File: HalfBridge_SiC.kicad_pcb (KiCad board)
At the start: 2 copper layers, 100 x 100.3 mm, 67 parts, among them J1 Conn_02x08_Odd_Even, J2 AFBR-2624Z, J3 AFBR-2624Z, J4 Screw_Terminal_01x02, J5 Conn_01x04_Shielded, Q1 C3M0075120J, Q2 C3M0075120J, SW1 CAS-D20X1, SW2 CAS-D20X1, SW3 CAS-D20X1, U1 RKD-052005D, U2 RKD-052005D, U3 MAX3284E, U4 NCD57252, U5 MAX3284E, U6 74AUC2GU04

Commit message: new optical diff xor
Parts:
- removed the C15 at (49.6, 100.6)
- removed the C17 at (49.5, 66.0)
- removed the C2 at (54.0, 86.5)
- removed the C3 at (54.0, 81.0)
- removed the J2 at (51.5, 61.9)
- removed the L1 at (44.5, 67.5)
- removed the R14 at (55.0, 51.6)
- removed the R15 at (54.9, 62.0)
- removed the R18 at (48.0, 85.5)
- removed SW3: CAS-D20X1, My_Button_Switch_SMD:Nidec_Copal_CAS-D20A1
- removed the U5 at (50.7, 80.0)
- removed the U6 at (53.0, 75.5)
- added C23: C, Capacitor_SMD:C_0805_2012Metric_Pad1.18x1.45mm_HandSolder, F.Cu at (46.0, 78.5)
- added C24: C, Capacitor_SMD:C_0805_2012Metric_Pad1.18x1.45mm_HandSolder, F.Cu at (45.0, 62.1)
- added C25: C, Capacitor_SMD:C_0805_2012Metric_Pad1.18x1.45mm_HandSolder, F.Cu at (45.0, 51.2)
- added C27: 100n, Capacitor_SMD:C_0603_1608Metric_Pad1.08x0.95mm_HandSolder, F.Cu at (22.8, 37.0)
- added C28: 100n, Capacitor_SMD:C_0603_1608Metric_Pad1.08x0.95mm_HandSolder, F.Cu at (22.8, 39.5)
- added C4: C, Capacitor_SMD:C_0603_1608Metric_Pad1.08x0.95mm_HandSolder, F.Cu at (49.6, 100.6)
- added D2: LED, LED_SMD:LED_0603_1608Metric_Pad1.05x0.95mm_HandSolder, F.Cu at (43.3, 95.5)
- added D3: LED, LED_SMD:LED_0603_1608Metric_Pad1.05x0.95mm_HandSolder, F.Cu at (43.3, 99.5)
- added D4: LED, LED_SMD:LED_0603_1608Metric_Pad1.05x0.95mm_HandSolder, F.Cu at (43.3, 103.5)
- added J4: AFBR-2624Z, OptoDevice:Broadcom_AFBR-16xxZ_Vertical, B.Cu at (49.5, 50.2)
- added J6: Conn_01x04_Shielded, My_Connector:Samtec_T1M-04-X-SH-L_1x04-1SH_P1.0mm_Terminal_Horizontal_Latch, F.Cu at (32.7, 38.0)
- added J7: Conn_01x02, Connector_PinHeader_2.54mm:PinHeader_1x02_P2.54mm_Vertical_SMD_Pin1Right, B.Cu at (61.0, 56.0)
- added L3: L, Inductor_SMD:L_0603_1608Metric_Pad1.05x0.95mm_HandSolder, F.Cu at (43.5, 55.2)
- added L4: L, Inductor_SMD:L_0603_1608Metric_Pad1.05x0.95mm_HandSolder, F.Cu at (43.5, 76.0)
- added R20: R, Resistor_SMD:R_0603_1608Metric_Pad0.98x0.95mm_HandSolder, F.Cu at (52.0, 51.2)
- added R21: R, Resistor_SMD:R_0603_1608Metric_Pad0.98x0.95mm_HandSolder, F.Cu at (52.0, 72.5)
- added R22: R, Resistor_SMD:R_0603_1608Metric_Pad0.98x0.95mm_HandSolder, F.Cu at (22.8, 42.0)
- added R23: R, Resistor_SMD:R_0603_1608Metric_Pad0.98x0.95mm_HandSolder, F.Cu at (22.8, 44.6)
- added R4: R, Resistor_SMD:R_0603_1608Metric, F.Cu at (45.0, 95.0)
- added R5: R, Resistor_SMD:R_0603_1608Metric, F.Cu at (45.0, 99.2)
- added R6: R, Resistor_SMD:R_0603_1608Metric, F.Cu at (45.0, 103.0)
- added U1: 74AHC1G86, Package_TO_SOT_SMD:SOT-23-5_HandSoldering, F.Cu at (52.0, 88.5)
- added U2: 74AHC1G86, Package_TO_SOT_SMD:SOT-23-5_HandSoldering, F.Cu at (48.0, 88.5)
- added U7: MAX3284E, Package_TO_SOT_SMD:SOT-23-6_Handsoldering, B.Cu at (29.6, 62.5)
- added U8: MAX3284E, Package_TO_SOT_SMD:SOT-23-6_Handsoldering, F.Cu at (55.1, 55.5)
- C18, C19: footprint Capacitor_SMD:C_0805_2012Metric_Pad1.18x1.45mm_HandSolder -> Capacitor_SMD:C_0603_1608Metric_Pad1.08x0.95mm_HandSolder
- C26: value 100n -> C; footprint Capacitor_SMD:C_0603_1608Metric_Pad1.08x0.95mm_HandSolder -> Capacitor_SMD:C_0805_2012Metric_Pad1.18x1.45mm_HandSolder
- J3: footprint OptoDevice:Broadcom_AFBR-16xxZ_Horizontal -> OptoDevice:Broadcom_AFBR-16xxZ_Vertical
- J5: value Conn_01x04_Shielded -> AFBR-2624Z; footprint My_Connector:Samtec_T1M-04-X-SH-L_1x04-1SH_P1.0mm_Terminal_Horizontal_Latch -> OptoDevice:Broadcom_AFBR-16xxZ_Vertical; moved to B.Cu
- R19: moved to F.Cu
- U3: value MAX3284E -> 74AHC1G86; footprint Package_TO_SOT_SMD:SOT-23-6_Handsoldering -> Package_TO_SOT_SMD:SOT-23-5_HandSoldering
- moved SW2 34.2 mm to (43.5, 109.2), turned to 90 degrees
- moved C20 19.5 mm to (48.0, 75.0)
- moved R19 18.4 mm to (52.0, 62.1)
- moved C21 12.7 mm to (46.0, 68.1), turned to -90 degrees
- moved J5 12.4 mm to (49.5, 71.4), turned to 180 degrees
- moved C26 12.2 mm to (45.0, 72.5), turned to 0 degrees
- moved C19 12.1 mm to (48.0, 53.7)
- moved J3 9.46 mm to (49.5, 60.9)
- moved L2 8.56 mm to (43.5, 65.6), turned to 90 degrees
- moved U3 7.30 mm to (44.0, 88.5), turned to -90 degrees
- moved C22 5.06 mm to (46.0, 57.7), turned to -90 degrees
- moved R9 3.13 mm to (47.2, 107.5), turned to 90 degrees
- moved SW1 2.05 mm to (43.5, 115.0)
- moved C18 1.46 mm to (48.0, 64.6)
- moved C16 0.50 mm to (66.0, 100.0)
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- renumbered C9 to C10, C10 to C11, C7 to C12, C8 to C13, C13 to C14, C14 to C15, C11 to C16, C12 to C17, C4 to C2, C5 to C3, C16 to C5, C23 to C6, C24 to C7, C6 to C8, C25 to C9, D3 to D1, D1 to D5, D2 to D6, J4 to J1, J1 to J2, L3 to L1, R17 to R1, R11 to R10, R3 to R11, R4 to R12, R5 to R13, R6 to R14, R7 to R15, R8 to R16, R9 to R17, R10 to R18, R1 to R2, R2 to R3, R12 to R7, R13 to R8, R16 to R9, U1 to U4, U4 to U5, U2 to U6
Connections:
- C19 pad 1: /HalfBridge_Diff/vcc -> /HalfBridge_Optical/vcca
- C20 pad 1: /HalfBridge_Optical/vcca -> /HalfBridge_Optical/vccen
- C21 pad 1: /HalfBridge_Optical/vcca -> /HalfBridge_Optical/vccb
- C22 pad 1: /HalfBridge_Diff/vcc -> /HalfBridge_Optical/vcca
- C26 pad 1: /HalfBridge_Diff/gnd -> /HalfBridge_Diff/vcc
- C26 pad 2: /HalfBridge_Diff/vcc -> /HalfBridge_Diff/gnd
- C9 pad 1: /HalfBridge_GateDriver/rdt -> /HalfBridge_GateDriver/dt
- J3 pad 1: /HalfBridge_Optical/xna -> /HalfBridge_Optical/oinb
- J3 pad 3: /HalfBridge_Optical/vcca -> /HalfBridge_Optical/vccb
- J5 pad 1: /HalfBridge_Diff/inb_db -> /HalfBridge_Optical/oinen
- J5 pad 2: /HalfBridge_Diff/inb_da -> /HalfBridge_Diff/gnd
- J5 pad 3: /HalfBridge_Diff/ina_db -> /HalfBridge_Optical/vccen
- J5 pad 4: /HalfBridge_Diff/ina_da -> unconnected-(J5-NC-Pad4)
- L2 pad 1: /HalfBridge_Optical/vcca -> /HalfBridge_Optical/vccb
- R19 pad 1: /HalfBridge_Diff/inb_da -> /HalfBridge_GateDriver/inb
- R19 pad 2: /HalfBridge_Diff/inb_db -> /HalfBridge_Optical/oinb
- R7 pad 1: /HalfBridge_GateDriver/ina -> /HalfBridge_GateDriver/inga
- R8 pad 1: /HalfBridge_GateDriver/inb -> /HalfBridge_GateDriver/ingb
- SW2 pad 1: /HalfBridge_Diff/ina_d -> /HalfBridge_Diff/vcc
- SW2 pad 2: /HalfBridge_GateDriver/ina -> /HalfBridge_GateDriver/dis_i
- SW2 pad 3: /HalfBridge_Optical/ina -> /HalfBridge_Diff/gnd
- SW2 pad 4: /HalfBridge_Diff/inb_d -> /HalfBridge_GateDriver/dis_x
- SW2 pad 5: /HalfBridge_GateDriver/inb -> /HalfBridge_GateDriver/dis
- SW2 pad 6: /HalfBridge_Optical/inb -> /HalfBridge_GateDriver/dis_i
- U3 pad 1: /HalfBridge_Diff/vcc -> /HalfBridge_GateDriver/en
- U3 pad 2: /HalfBridge_Diff/gnd -> unconnected-(U3-Pad2)
- U3 pad 3: /HalfBridge_Diff/ina_nd -> /HalfBridge_Diff/gnd
- U3 pad 4: /HalfBridge_Diff/ina_db -> /HalfBridge_GateDriver/dis_x
- U3 pad 5: unconnected-(U3-VL-Pad5) -> /HalfBridge_Diff/vcc
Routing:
- net /HalfBridge_Diff/vcc: track 152.6 -> 14.4 mm
- net /HalfBridge_GateDriver/ina: track 10.2 -> 48.5 mm
- net /HalfBridge_Optical/ina: track 31.2 -> 0.00 mm
- net /HalfBridge_GateDriver/en: track 0.00 -> 23.6 mm
- net /HalfBridge_Optical/inb: track 20.7 -> 0.00 mm
- net /HalfBridge_GateDriver/inb: track 17.9 -> 36.3 mm
- net /HalfBridge_Diff/inb_d: track 12.5 -> 0.00 mm
- net /HalfBridge_GateDriver/dis: track 0.00 -> 12.3 mm
- net /HalfBridge_GateDriver/dt: track 0.00 -> 11.9 mm
- net /HalfBridge_Diff/ina_nd: track 9.15 -> 0.00 mm
- net /HalfBridge_GateDriver/inga: track 0.00 -> 9.08 mm
- net /HalfBridge_Diff/inb_nd: track 5.86 -> 0.00 mm
- net /HalfBridge_GateDriver/ingb: track 0.00 -> 5.50 mm
- net /HalfBridge_GateDriver/anb: track 0.00 -> 5.38 mm
- net /HalfBridge_GateDriver/dis_i: track 0.00 -> 3.52 mm
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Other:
- board text removed: "INA PWM"
- board text removed: "INB"

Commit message: diff circuit
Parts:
- removed J6: Conn_01x04_Shielded, My_Connector:Samtec_T1M-04-X-SH-L_1x04-1SH_P1.0mm_Terminal_Horizontal_Latch
- added C12: 100n, Capacitor_SMD:C_0603_1608Metric_Pad1.08x0.95mm_HandSolder, F.Cu at (52.0, 115.0)
- added C33: 100n, Capacitor_SMD:C_0603_1608Metric_Pad1.08x0.95mm_HandSolder, F.Cu at (64.0, 78.5)
- added C4: 100n, Capacitor_SMD:C_0603_1608Metric_Pad1.08x0.95mm_HandSolder, F.Cu at (51.5, 92.0)
- added C5: 100n, Capacitor_SMD:C_0603_1608Metric_Pad1.08x0.95mm_HandSolder, F.Cu at (47.5, 92.0)
- added C6: 100n, Capacitor_SMD:C_0603_1608Metric_Pad1.08x0.95mm_HandSolder, F.Cu at (43.5, 92.0)
- added J10: Conn_01x02, Connector_PinHeader_2.54mm:PinHeader_1x02_P2.54mm_Vertical, F.Cu at (63.5, 50.7)
- added J11: Conn_01x02, Connector_PinHeader_2.54mm:PinHeader_1x02_P2.54mm_Vertical, F.Cu at (63.5, 61.2)
- added J12: Conn_01x02, Connector_PinHeader_2.54mm:PinHeader_1x02_P2.54mm_Vertical, F.Cu at (63.5, 72.2)
- added J14: Conn_01x02_Shielded, My_Connector:SAMTEC_T1M-02-F-SV-L-P, B.Cu at (60.4, 67.7)
- added J8: Conn_01x02, Connector_PinHeader_2.54mm:PinHeader_1x02_P2.54mm_Vertical, F.Cu at (54.0, 66.2)
- added J9: Conn_01x02, Connector_PinHeader_2.54mm:PinHeader_1x02_P2.54mm_Vertical, F.Cu at (54.0, 76.7)
- added R24: R, Resistor_SMD:R_0603_1608Metric_Pad0.98x0.95mm_HandSolder, F.Cu at (57.0, 78.5)
- added R25: R, Resistor_SMD:R_0603_1608Metric, F.Cu at (60.5, 52.5)
- added R26: R, Resistor_SMD:R_0603_1608Metric, F.Cu at (60.5, 63.0)
- added R27: R, Resistor_SMD:R_0603_1608Metric, F.Cu at (60.5, 74.0)
- added U9: MAX3284E, Package_TO_SOT_SMD:SOT-23-6_Handsoldering, F.Cu at (60.5, 78.5)
- J7: footprint Connector_PinHeader_2.54mm:PinHeader_1x02_P2.54mm_Vertical_SMD_Pin1Right -> Connector_PinHeader_2.54mm:PinHeader_1x02_P2.54mm_Vertical; moved to F.Cu
- U7: moved to F.Cu
- moved C32 50.1 mm to (64.0, 68.0), turned to 90 degrees
- moved C31 46.0 mm to (64.0, 57.5), turned to 90 degrees
- moved R23 41.5 mm to (57.0, 68.0), turned to 90 degrees
- moved R22 37.6 mm to (57.0, 57.5), turned to 90 degrees
- moved U7 31.1 mm to (60.4, 57.5)
- moved U8 13.6 mm to (60.5, 68.0), turned to 180 degrees
- moved J7 7.04 mm to (54.0, 55.2), turned to 0 degrees
- moved D5 2.50 mm to (72.5, 89.3)
- moved D6 2.00 mm to (72.5, 128.0)
- moved U1 1.50 mm to (50.5, 88.5)
- moved U2 1.50 mm to (46.5, 88.5)
- moved U3 1.50 mm to (42.5, 88.5)
- moved R6 1.17 mm to (45.0, 104.2)
- moved D4 1.04 mm to (43.3, 104.5)
- moved D2 1.00 mm to (43.3, 96.5)
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- renumbered C7 to C10, C8 to C11, C9 to C13, C10 to C14, C11 to C15, C12 to C16, C13 to C17, C14 to C18, C15 to C19, C16 to C20, C17 to C21, C18 to C22, C19 to C23, C20 to C24, C21 to C25, C22 to C26, C23 to C27, C24 to C28, C25 to C29, C26 to C30, C27 to C31, C28 to C32, C4 to C7, C5 to C8, C6 to C9
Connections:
- net /HalfBridge_GateDriver/en renamed /HalfBridge_Diff/inen_d
- net /HalfBridge_GateDriver/ina renamed /HalfBridge_Diff/ina_d
- net /HalfBridge_GateDriver/inb renamed /HalfBridge_Diff/inb_d
- J7 pad 1: unconnected-(J7-Pin_1-Pad1) -> /HalfBridge_Diff/ina_db
- J7 pad 2: unconnected-(J7-Pin_2-Pad2) -> /HalfBridge_Diff/ina_da
- SW2 pad 1: /HalfBridge_Diff/vcc -> /HalfBridge_GateDriver/dis_i
- SW2 pad 2: /HalfBridge_GateDriver/dis_i -> /HalfBridge_GateDriver/dis
- SW2 pad 3: /HalfBridge_Diff/gnd -> /HalfBridge_GateDriver/dis_x
- SW2 pad 4: /HalfBridge_GateDriver/dis_x -> /HalfBridge_Diff/gnd
- SW2 pad 5: /HalfBridge_GateDriver/dis -> /HalfBridge_GateDriver/dis_i
- SW2 pad 6: /HalfBridge_GateDriver/dis_i -> /HalfBridge_Diff/vcc
- U7 pad 5: unconnected-(U7-VL-Pad5) -> /HalfBridge_Diff/vcc
- U8 pad 5: unconnected-(U8-VL-Pad5) -> /HalfBridge_Diff/vcc
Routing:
- net /HalfBridge_Diff/vcc: track 14.4 -> 138.5 mm
- net /HalfBridge_GateDriver/dis_x: track 2.05 -> 18.0 mm
- net /HalfBridge_GateDriver/ingb: track 5.50 -> 21.4 mm
- net /HalfBridge_GateDriver/inga: track 9.08 -> 18.5 mm
- net /HalfBridge_GateDriver/anb: track 5.38 -> 12.2 mm
- net /HalfBridge_Diff/inen_d: track 23.6 -> 20.3 mm
- net /HalfBridge_GateDriver/asgh: track 6.56 -> 4.06 mm
- net /HalfBridge_Diff/ina_d: track 48.5 -> 50.8 mm
- net /HalfBridge_GateDriver/asgl: track 4.27 -> 2.06 mm
- net /HalfBridge_Diff/inb_d: track 36.3 -> 37.8 mm
- net /HalfBridge_GateDriver/dis: track 12.3 -> 13.4 mm
- net /HalfBridge_GateDriver/kl: vias 24 -> 26
- net /HalfBridge_Diff/gnd: vias 0 -> 4
- added copper zone on B.Cu, net /HalfBridge_Diff/gnd
- added copper zone on F.Cu, net /HalfBridge_Diff/gnd
- removed copper zone on B.Cu, net (none)
- removed copper zone on F.Cu, net (none)
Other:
- board size 100 x 100.3 mm -> 100 x 100 mm

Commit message: pcb position
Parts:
- C18, C19, R4, R5, R6: moved to B.Cu
- moved C9 7.38 mm to (50.0, 102.5), turned to 180 degrees
- moved C18 7.02 mm to (66.0, 110.5), turned to 0 degrees
- moved C19 6.02 mm to (66.0, 113.5)
- moved R4 2.92 mm to (42.5, 97.5)
- moved R5 2.69 mm to (42.5, 101.0)
- moved R6 2.52 mm to (42.5, 104.5)
- moved U6 2.19 mm to (50.9, 121.6)
- moved R13 2.00 mm to (75.5, 91.8)
- moved R14 2.00 mm to (75.5, 93.8)
- moved L1 1.93 mm to (51.0, 105.6), turned to -90 degrees
- moved R1 1.66 mm to (44.0, 123.0), turned to 90 degrees
- moved C10 1.58 mm to (51.0, 109.5), turned to -90 degrees
- moved C4 1.00 mm to (51.5, 93.0)
- moved C5 1.00 mm to (47.5, 93.0)
- moved C6 1.00 mm to (43.5, 93.0)
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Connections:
- R1 pad 2: GND -> /HalfBridge_Diff/gnd
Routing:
- net /HalfBridge_Diff/inen_d: track 20.3 -> 47.9 mm
- net /HalfBridge_Diff/inb_d: track 37.8 -> 56.6 mm
- net /HalfBridge_Diff/vcc: track 138.5 -> 156.5 mm
- net /HalfBridge_GateDriver/vcci: track 0.00 -> 16.2 mm, vias 0 -> 3
- net /HalfBridge_GateDriver/vddl: track 2.18 -> 16.4 mm, vias 0 -> 2
- net /HalfBridge_Diff/ina_d: track 50.8 -> 64.8 mm
- net /HalfBridge_GateDriver/vssl: track 2.16 -> 8.23 mm, vias 0 -> 2
- net /HalfBridge_GateDriver/inaf: track 0.00 -> 4.98 mm
- net /HalfBridge_GateDriver/inbf: track 0.00 -> 4.04 mm
- net /HalfBridge_GateDriver/ingb: track 21.4 -> 17.7 mm
- net /HalfBridge_GateDriver/rdt: track 0.36 -> 3.84 mm
- net /HalfBridge_GateDriver/gonl: track 24.8 -> 26.9 mm
- net /HalfBridge_GateDriver/dt: track 11.5 -> 13.3 mm
- net /HalfBridge_GateDriver/dis_x: track 18.0 -> 17.0 mm
- net /HalfBridge_GateDriver/inga: track 18.5 -> 17.9 mm
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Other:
- outline, holes or cut-outs redrawn

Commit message: route
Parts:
- moved J14 4.09 mm to (64.5, 68.0), turned to -90 degrees
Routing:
- net /HalfBridge_GateDriver/gonh: track 7.32 -> 23.6 mm
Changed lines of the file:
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@@
 		(tags "capacitor handsolder")
 		(property "Reference" "C18"
-			(at 0 -1.945 360)
+			(at 0 -1.945 0)
 			(layer "B.SilkS")
 			(effects
@@
 		)
 		(property "Value" "C"
-			(at 0 -1.68 360)
+			(at 0 -1.68 0)
 			(layer "B.Fab")
 			(effects
@@
 		)
 		(fp_text user "${REFERENCE}"
-			(at 0 0 360)
+			(at 0 0 0)
 			(layer "B.Fab")
 			(effects
@@
 		)
 		(property "Value" "C"
-			(at 0 -1.68 360)
+			(at 0 -1.68 0)
 			(layer "B.Fab")
 			(effects
@@
 		)
 		(fp_text user "${REFERENCE}"
-			(at 0 0 360)
+			(at 0 0 0)
 			(layer "B.Fab")
 			(effects
@@
 	(footprint "My_Connector:SAMTEC_T1M-02-F-SV-L-P"
 		(layer "B.Cu")
-		(at 60.425 67.7 90)
+		(at 64.5 68 -90)
 		(descr "1MM TERMINAL STRIP, 5PINS.")
 		(property "Reference" "J14"
@@
 		(attr smd)
 		(fp_line
-			(start 2.2 0.425)
-			(end 2.2 1.3)
+			(start -1 4.375)
+			(end -1 3.175)
 			(stroke
 				(width 0.127)
@@
 		)
 		(fp_line
-			(start 1.25 0.425)
-			(end 1.25 -0.075)
+			(start 1 4.375)
+			(end -1 4.375)
 			(stroke
 				(width 0.127)
@@
 		)
 		(fp_line
-			(start 1.25 0.425)
-			(end 2.2 0.425)
+			(start 1 4.375)
+			(end 1 3.175)
 			(stroke
 				(width 0.127)
@@
 		)
 		(fp_line
-			(start -1.25 0.425)
-			(end -1.25 -0.075)
+			(start -2.2 0.425)
+			(end -2.2 1.3)
 			(stroke
 				(width 0.127)
@@
 		)
 		(fp_line
-			(start -2.2 0.425)
-			(end -2.2 1.3)
+			(start -1.25 0.425)
+			(end -1.25 -0.075)
 			(stroke
 				(width 0.127)
@@
 		)
 		(fp_line
-			(start 1 4.375)
-			(end 1 3.175)
+			(start 1.25 0.425)
+			(end 2.2 0.425)
 			(stroke
 				(width 0.127)
@@
 		)
 		(fp_line
-			(start 1 4.375)
-			(end -1 4.375)
+			(start 1.25 0.425)
+			(end 1.25 -0.075)
 			(stroke
 				(width 0.127)
@@
 		)
 		(fp_line
-			(start -1 4.375)
-			(end -1 3.175)
+			(start 2.2 0.425)
+			(end 2.2 1.3)
 			(stroke
 				(width 0.127)
@@
 		)
 		(fp_line
-			(start 2.45 -1.025)
-			(end 2.45 4.625)
+			(start -2.45 4.625)
+			(end -2.45 -1.025)
 			(stroke
 				(width 0.05)
@@
 		)
 		(fp_line
-			(start -2.45 -1.025)
-			(end 2.45 -1.025)
+			(start 2.45 4.625)
+			(end -2.45 4.625)
 			(stroke
 				(width 0.05)
@@
 		)
 		(fp_line
-			(start 2.45 4.625)
-			(end -2.45 4.625)
+			(start -2.45 -1.025)
+			(end 2.45 -1.025)
 			(stroke
 				(width 0.05)
@@
 		)
 		(fp_line
-			(start -2.45 4.625)
-			(end -2.45 -1.025)
+			(start 2.45 -1.025)
+			(end 2.45 4.625)
 			(stroke
 				(width 0.05)
@@
 		)
 		(fp_line
-			(start 1.25 -0.075)
-			(end 1.25 0.425)
+			(start -1 4.375)
+			(end -1 3.175)
 			(stroke
 				(width 0.127)
@@
 		)
 		(fp_line
-			(start -1.25 -0.075)
-			(end 1.25 -0.075)
+			(start 1 4.375)
+			(end -1 4.375)
 			(stroke
 				(width 0.127)
@@
 		)
 		(fp_line
-			(start 2.2 0.425)
-			(end 2.2 3.175)
+			(start -2.2 3.175)
+			(end -2.2 0.425)
 			(stroke
 				(width 0.127)
@@
 		)
 		(fp_line
-			(start 1.25 0.425)
-			(end 2.2 0.425)
+			(start -1 3.175)
+			(end -2.2 3.175)
 			(stroke
 				(width 0.127)
@@
 		)
 		(fp_line
-			(start -1.25 0.425)
-			(end -1.25 -0.075)
+			(start 1 3.175)
+			(end 1 4.375)
 			(stroke
 				(width 0.127)
@@
 		)
 		(fp_line
-			(start -2.2 0.425)
-			(end -1.25 0.425)
+			(start 2.2 3.175)
+			(end 1 3.175)
 			(stroke
 				(width 0.127)
@@
 		)
 		(fp_line
-			(start 2.2 3.175)
-			(end 1 3.175)
+			(start -2.2 0.425)
+			(end -1.25 0.425)
 			(stroke
 				(width 0.127)
@@
 		)
 		(fp_line
-			(start 1 3.175)
-			(end 1 4.375)
+			(start -1.25 0.425)
+			(end -1.25 -0.075)
 			(stroke
 				(width 0.127)
@@
 		)
 		(fp_line
-			(start -1 3.175)
-			(end -2.2 3.175)
+			(start 1.25 0.425)
+			(end 2.2 0.425)
 			(stroke
 				(width 0.127)
@@
 		)
 		(fp_line
-			(start -2.2 3.175)
-			(end -2.2 0.425)
+			(start 2.2 0.425)
+			(end 2.2 3.175)
 			(stroke
 				(width 0.127)
@@
 		)
 		(fp_line
-			(start 1 4.375)
-			(end -1 4.375)
+			(start -1.25 -0.075)
+			(end 1.25 -0.075)
 			(stroke
 				(width 0.127)
@@
 		)
 		(fp_line
-			(start -1 4.375)
-			(end -1 3.175)
+			(start 1.25 -0.075)
+			(end 1.25 0.425)
 			(stroke
 				(width 0.127)
@@
 		)
 		(pad "1" smd rect
-			(at -0.5 0 90)
+			(at -0.5 0 270)
 			(size 0.6 1.55)
 			(layers "B.Cu" "B.Paste" "B.Mask")
@@
 		)
 		(pad "2" smd rect
-			(at 0.5 0 90)
+			(at 0.5 0 270)
 			(size 0.6 1.55)
 			(layers "B.Cu" "B.Paste" "B.Mask")
@@
 		)
 		(pad "SH" smd rect
-			(at -1.8 2.575 90)
+			(at -1.8 2.575 270)
 			(size 0.8 1.8)
 			(layers "B.Cu" "B.Paste" "B.Mask")
@@
 		)
 		(pad "SH" smd rect
-			(at 1.8 2.575 90)
+			(at 1.8 2.575 270)
 			(size 0.8 1.8)
 			(layers "B.Cu" "B.Paste" "B.Mask")
@@
 		(tags "capacitor handsolder")
 		(property "Reference" "C19"
-			(at 0 -1.945 360)
+			(at 0 -1.945 0)
 			(layer "B.SilkS")
 			(effects
@@
 		)
 		(property "Value" "C"
-			(at 0 -1.68 360)
+			(at 0 -1.68 0)
 			(layer "B.Fab")
 			(effects
@@
 		)
 		(fp_text user "${REFERENCE}"
-			(at 0 0 360)
+			(at 0 0 0)
 			(layer "B.Fab")
 			(effects
@@
 	)
 	(segment
+		(start 72 95.5)
+		(end 73.68 93.82)
+		(width 0.6)
+		(layer "F.Cu")
+		(net 8)
+	)
+	(segment
 		(start 62.8 105.63)
-		(end 68.12 105.63)
+		(end 70.37 105.63)
+		(width 0.6)
+		(layer "F.Cu")
+		(net 8)
+	)
+	(segment
+		(start 70.37 105.63)
+		(end 72 104)
 		(width 0.6)
 		(layer "F.Cu")
@@
 	)
 	(segment
+		(start 73.68 93.82)
+		(end 74.5 93.82)
+		(width 0.6)
+		(layer "F.Cu")
+		(net 8)
+	)
+	(segment
+		(start 72 104)
+		(end 72 95.5)
+		(width 0.6)
+		(layer "F.Cu")
+		(net 8)
+	)
+	(segment
 		(start 70.5 113)
 		(end 70.5 122.5)
@@
 		(polygon
 			(pts
-				(xy 61 109.945) (xy 70.85 109.945) (xy 70.85 122.445) (xy 81 122.5) (xy 81 132.5) (xy 61 132.5)
+				(xy 61 109.945) (xy 70.85 109.945) (xy 70.85 122.445) (xy 81 122.5) (xy 81 133) (xy 61 133)
 			)
 		)

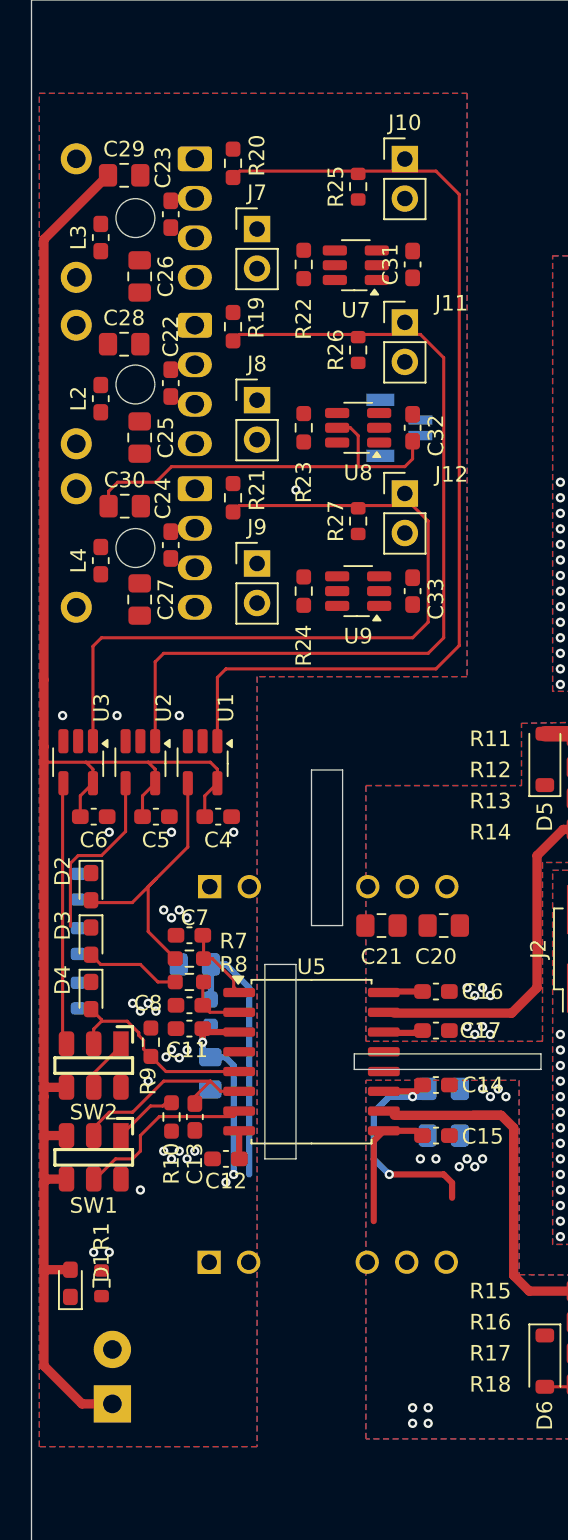
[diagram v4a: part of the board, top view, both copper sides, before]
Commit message: horizontal connector
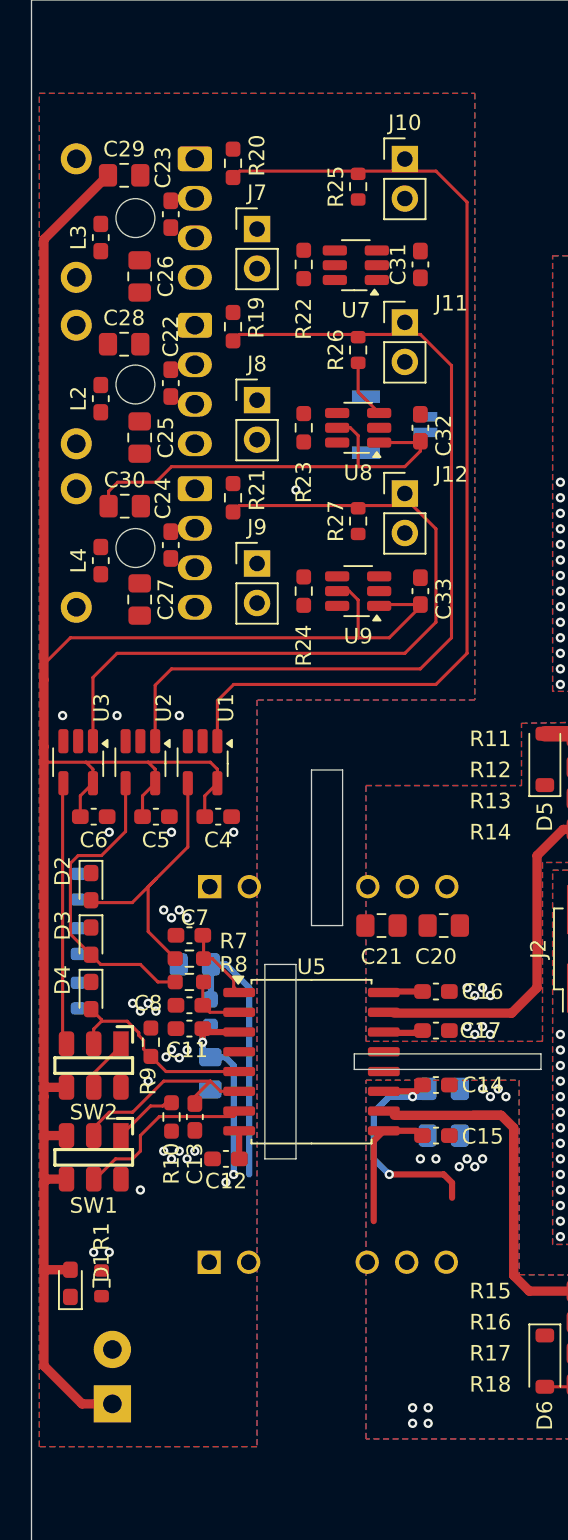
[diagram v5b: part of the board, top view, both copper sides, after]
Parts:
- J14: footprint My_Connector:SAMTEC_T1M-02-F-SV-L-P -> My_Connector:SAMTEC_T1M-02-F-SH-L-K
- moved C31 0.50 mm to (64.5, 57.5)
- moved C32 0.50 mm to (64.5, 68.0)
- moved C33 0.50 mm to (64.5, 78.5)
- moved J14 0.25 mm to (64.7, 67.8), turned to 90 degrees
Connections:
- J14 pad 1: /HalfBridge_Diff/inb_db -> /HalfBridge_Diff/inb_da
- J14 pad 2: /HalfBridge_Diff/inb_da -> /HalfBridge_Diff/inb_db
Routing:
- net /HalfBridge_Diff/vcc: track 156.5 -> 193.0 mm
- net /HalfBridge_Diff/inb_nd: track 0.00 -> 3.78 mm
- net /HalfBridge_GateDriver/ingb: track 17.7 -> 20.1 mm
